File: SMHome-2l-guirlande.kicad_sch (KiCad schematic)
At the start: 12 parts, among them J1 Screw_Terminal_01x02, SW1 SW_Push, U2 VS1838B, U3 ESP32-C3 Pro Mini, U5 FAN8082

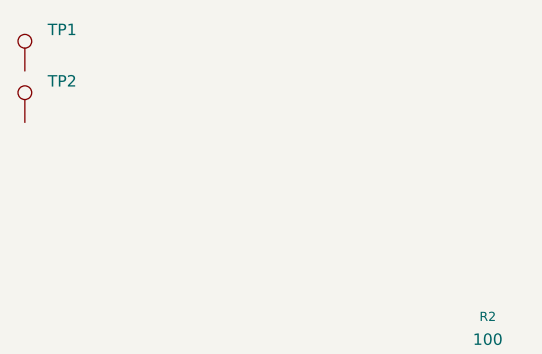
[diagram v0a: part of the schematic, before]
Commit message: Decrease size. Center BTN
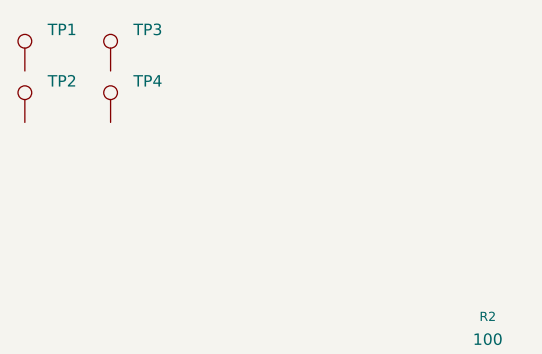
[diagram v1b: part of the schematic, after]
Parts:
- added TP3, TP4: ~, MountingHole:MountingHole_2.1mm, symbol Connector:TestPoint
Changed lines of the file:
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@@
+	)
+	(symbol
+		(lib_id "Connector:TestPoint")
+		(at 40.005 35.56 0)
+		(unit 1)
+		(exclude_from_sim no)
+		(in_bom yes)
+		(on_board yes)
+		(dnp no)
+		(fields_autoplaced yes)
+		(property "Reference" "TP4"
+			(at 42.545 30.9879 0)
+			(effects
+				(font
+					(size 1.27 1.27)
+				)
+				(justify left)
+			)
+		)
+		(property "Value" "~"
+			(at 42.545 33.5279 0)
+			(effects
+				(font
+					(size 1.27 1.27)
+				)
+				(justify left)
+			)
+		)
+		(property "Footprint" "MountingHole:MountingHole_2.1mm"
+			(at 45.085 35.56 0)
+			(effects
+				(font
+					(size 1.27 1.27)
+				)
+				(hide yes)
+			)
+		)
+		(property "Datasheet" "~"
+			(at 45.085 35.56 0)
+			(effects
+				(font
+					(size 1.27 1.27)
+				)
+				(hide yes)
+			)
+		)
+		(property "Description" "test point"
+			(at 40.005 35.56 0)
+			(effects
+				(font
+					(size 1.27 1.27)
+				)
+				(hide yes)
+			)
+		)
+		(property "descr" ""
+			(at 40.005 35.56 0)
+			(effects
+				(font
+					(size 1.27 1.27)
+				)
+			)
+		)
+		(pin "1"
+		)
+		(instances
+			(project "SMHome-2l-guirlande"
+				(path "/3ad76f73-bf60-4bf6-a476-23c2ee94149d"
+					(reference "TP4")
+					(unit 1)
+				)
+			)
+		)
 	)
 	(symbol
@@
 					(unit 1)
 				)
+			)
+		)
+	)
+	(symbol
+		(lib_id "Connector:TestPoint")
+		(at 40.005 29.845 0)
+		(unit 1)
+		(exclude_from_sim no)
+		(in_bom yes)
+		(on_board yes)
+		(dnp no)
+		(fields_autoplaced yes)
+		(property "Reference" "TP3"
+			(at 42.545 25.2729 0)
+			(effects
+				(font
+					(size 1.27 1.27)
+				)
+				(justify left)
+			)
+		)
+		(property "Value" "~"
+			(at 42.545 27.8129 0)
+			(effects
+				(font
+					(size 1.27 1.27)
+				)
+				(justify left)
+			)
+		)
+		(property "Footprint" "MountingHole:MountingHole_2.1mm"
+			(at 45.085 29.845 0)
+			(effects
+				(font
+					(size 1.27 1.27)
+				)
+				(hide yes)
+			)
+		)
+		(property "Datasheet" "~"
+			(at 45.085 29.845 0)
+			(effects
+				(font
+					(size 1.27 1.27)
+				)
+				(hide yes)
+			)
+		)
+		(property "Description" "test point"
+			(at 40.005 29.845 0)
+			(effects
+				(font
+					(size 1.27 1.27)
+				)
+				(hide yes)
+			)
+		)
+		(property "descr" ""
+			(at 40.005 29.845 0)
+			(effects
+				(font
+					(size 1.27 1.27)
+				)
+			)
+		)
+		(pin "1"
+		)
+		(instances
+			(project "SMHome-2l-guirlande"
+				(path "/3ad76f73-bf60-4bf6-a476-23c2ee94149d"
+					(reference "TP3")
+					(unit 1)
+				)

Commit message: Make assemble documents. make narrower
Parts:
- TP1, TP2, TP3, TP4: symbol Connector:TestPoint -> Mechanical:MountingHole; now left out of the parts list
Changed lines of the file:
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@@
 	)
 	(symbol
-		(lib_id "Connector:TestPoint")
+		(lib_id "Mechanical:MountingHole")
 		(at 30.48 29.845 0)
 		(unit 1)
 		(exclude_from_sim no)
-		(in_bom yes)
+		(in_bom no)
 		(on_board yes)
 		(dnp no)
 		(fields_autoplaced yes)
 		(property "Reference" "TP1"
-			(at 33.02 25.2729 0)
+			(at 33.02 28.5749 0)
 			(effects
 				(font
@@
 		)
 		(property "Value" "~"
-			(at 33.02 27.8129 0)
+			(at 33.02 31.1149 0)
 			(effects
 				(font
@@
 		)
 		(property "Footprint" "MountingHole:MountingHole_2.1mm"
-			(at 35.56 29.845 0)
+			(at 30.48 29.845 0)
 			(effects
 				(font
@@
 		)
 		(property "Datasheet" "~"
-			(at 35.56 29.845 0)
-			(effects
-				(font
-					(size 1.27 1.27)
-				)
-				(hide yes)
-			)
-		)
-		(property "Description" "test point"
 			(at 30.48 29.845 0)
 			(effects
@@
 			)
 		)
-		(property "descr" ""
+		(property "Description" "Mounting Hole without connection"
 			(at 30.48 29.845 0)
 			(effects
@@
 					(size 1.27 1.27)
 				)
-			)
-		)
-		(pin "1"
+				(hide yes)
+			)
+		)
+		(property "descr" ""
+			(at 30.48 29.845 0)
+			(effects
+				(font
+					(size 1.27 1.27)
+				)
+			)
 		)
 		(instances
@@
 	)
 	(symbol
-		(lib_id "Connector:TestPoint")
+		(lib_id "Mechanical:MountingHole")
 		(at 40.005 35.56 0)
 		(unit 1)
 		(exclude_from_sim no)
-		(in_bom yes)
+		(in_bom no)
 		(on_board yes)
 		(dnp no)
 		(fields_autoplaced yes)
 		(property "Reference" "TP4"
-			(at 42.545 30.9879 0)
+			(at 43.18 34.2899 0)
 			(effects
 				(font
@@
 		)
 		(property "Value" "~"
-			(at 42.545 33.5279 0)
+			(at 43.18 36.8299 0)
 			(effects
 				(font
@@
 		)
 		(property "Footprint" "MountingHole:MountingHole_2.1mm"
-			(at 45.085 35.56 0)
+			(at 40.005 35.56 0)
 			(effects
 				(font
@@
 		)
 		(property "Datasheet" "~"
-			(at 45.085 35.56 0)
-			(effects
-				(font
-					(size 1.27 1.27)
-				)
-				(hide yes)
-			)
-		)
-		(property "Description" "test point"
 			(at 40.005 35.56 0)
 			(effects
@@
 			)
 		)
-		(property "descr" ""
+		(property "Description" "Mounting Hole without connection"
 			(at 40.005 35.56 0)
 			(effects
@@
 					(size 1.27 1.27)
 				)
-			)
-		)
-		(pin "1"
+				(hide yes)
+			)
+		)
+		(property "descr" ""
+			(at 40.005 35.56 0)
+			(effects
+				(font
+					(size 1.27 1.27)
+				)
+			)
 		)
 		(instances
@@
 	)
 	(symbol
-		(lib_id "Connector:TestPoint")
+		(lib_id "Mechanical:MountingHole")
 		(at 30.48 35.56 0)
 		(unit 1)
 		(exclude_from_sim no)
-		(in_bom yes)
+		(in_bom no)
 		(on_board yes)
 		(dnp no)
 		(fields_autoplaced yes)
 		(property "Reference" "TP2"
-			(at 33.02 30.9879 0)
+			(at 33.02 34.2899 0)
 			(effects
 				(font
@@
 		)
 		(property "Value" "~"
-			(at 33.02 33.5279 0)
+			(at 33.02 36.8299 0)
 			(effects
 				(font
@@
 		)
 		(property "Footprint" "MountingHole:MountingHole_2.1mm"
-			(at 35.56 35.56 0)
+			(at 30.48 35.56 0)
 			(effects
 				(font
@@
 		)
 		(property "Datasheet" "~"
-			(at 35.56 35.56 0)
-			(effects
-				(font
-					(size 1.27 1.27)
-				)
-				(hide yes)
-			)
-		)
-		(property "Description" "test point"
 			(at 30.48 35.56 0)
 			(effects
@@
 			)
 		)
-		(property "descr" ""
+		(property "Description" "Mounting Hole without connection"
 			(at 30.48 35.56 0)
 			(effects
@@
 					(size 1.27 1.27)
 				)
-			)
-		)
-		(pin "1"
+				(hide yes)
+			)
+		)
+		(property "descr" ""
+			(at 30.48 35.56 0)
+			(effects
+				(font
+					(size 1.27 1.27)
+				)
+			)
 		)
 		(instances
@@
 	)
 	(symbol
-		(lib_id "Connector:TestPoint")
+		(lib_id "Mechanical:MountingHole")
 		(at 40.005 29.845 0)
 		(unit 1)
 		(exclude_from_sim no)
-		(in_bom yes)
+		(in_bom no)
 		(on_board yes)
 		(dnp no)
 		(fields_autoplaced yes)
 		(property "Reference" "TP3"
-			(at 42.545 25.2729 0)
+			(at 43.18 28.5749 0)
 			(effects
 				(font
@@
 		)
 		(property "Value" "~"
-			(at 42.545 27.8129 0)
+			(at 43.18 31.1149 0)
 			(effects
 				(font
@@
 		)
 		(property "Footprint" "MountingHole:MountingHole_2.1mm"
-			(at 45.085 29.845 0)
+			(at 40.005 29.845 0)
 			(effects
 				(font
@@
 		)
 		(property "Datasheet" "~"
-			(at 45.085 29.845 0)
-			(effects
-				(font
-					(size 1.27 1.27)
-				)
-				(hide yes)
-			)
-		)
-		(property "Description" "test point"
 			(at 40.005 29.845 0)
 			(effects
@@
 			)
 		)
-		(property "descr" ""
+		(property "Description" "Mounting Hole without connection"
 			(at 40.005 29.845 0)
 			(effects
@@
 					(size 1.27 1.27)
 				)
-			)
-		)
-		(pin "1"
-		)
-		(instances
+				(hide yes)
+			)
+		)
+		(property "descr" ""
+			(at 40.005 29.845 0)
+			(effects
+				(font
+					(size 1.27 1.27)
+				)
+			)
+		)
+		(instances

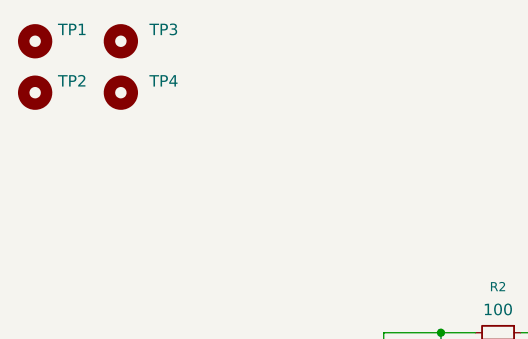
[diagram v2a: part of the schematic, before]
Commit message: Fix mounting holes. Move sensor
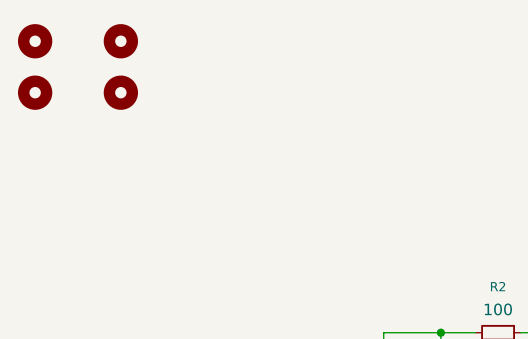
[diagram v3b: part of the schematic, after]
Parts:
- TP1, TP2, TP3, TP4: footprint MountingHole:MountingHole_2.1mm -> MountingHole:MountingHole_2.5mm
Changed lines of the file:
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@@
 				)
 				(justify left)
+				(hide yes)
 			)
 		)
@@
 				)
 				(justify left)
-			)
-		)
-		(property "Footprint" "MountingHole:MountingHole_2.1mm"
+				(hide yes)
+			)
+		)
+		(property "Footprint" "MountingHole:MountingHole_2.5mm"
 			(at 30.48 29.845 0)
 			(effects
@@
 					(size 1.27 1.27)
 				)
+				(hide yes)
 			)
 		)
@@
 				)
 				(justify left)
+				(hide yes)
 			)
 		)
@@
 				)
 				(justify left)
-			)
-		)
-		(property "Footprint" "MountingHole:MountingHole_2.1mm"
+				(hide yes)
+			)
+		)
+		(property "Footprint" "MountingHole:MountingHole_2.5mm"
 			(at 40.005 35.56 0)
 			(effects
@@
 					(size 1.27 1.27)
 				)
+				(hide yes)
 			)
 		)
@@
 				)
 				(justify left)
+				(hide yes)
 			)
 		)
@@
 				)
 				(justify left)
-			)
-		)
-		(property "Footprint" "MountingHole:MountingHole_2.1mm"
+				(hide yes)
+			)
+		)
+		(property "Footprint" "MountingHole:MountingHole_2.5mm"
 			(at 30.48 35.56 0)
 			(effects
@@
 					(size 1.27 1.27)
 				)
+				(hide yes)
 			)
 		)
@@
 				)
 				(justify left)
+				(hide yes)
 			)
 		)
@@
 				)
 				(justify left)
-			)
-		)
-		(property "Footprint" "MountingHole:MountingHole_2.1mm"
+				(hide yes)
+			)
+		)
+		(property "Footprint" "MountingHole:MountingHole_2.5mm"
 			(at 40.005 29.845 0)
 			(effects
@@
 					(size 1.27 1.27)
 				)
-			)
-		)
+				(hide yes)
+			)
+		)
